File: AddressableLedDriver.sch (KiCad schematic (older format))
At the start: 23 parts

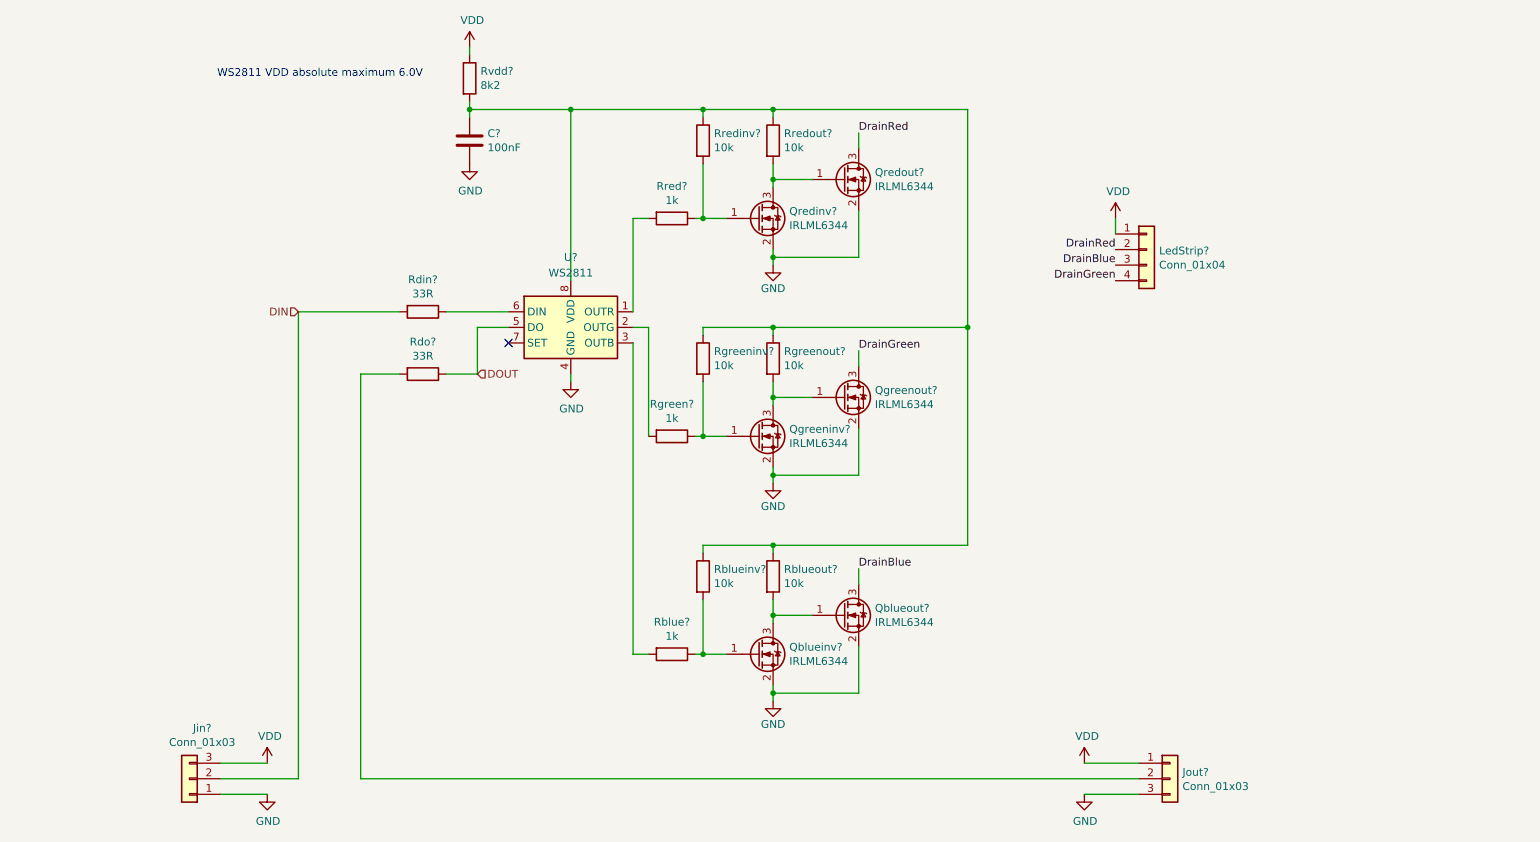
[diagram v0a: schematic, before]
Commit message: Restructure schema
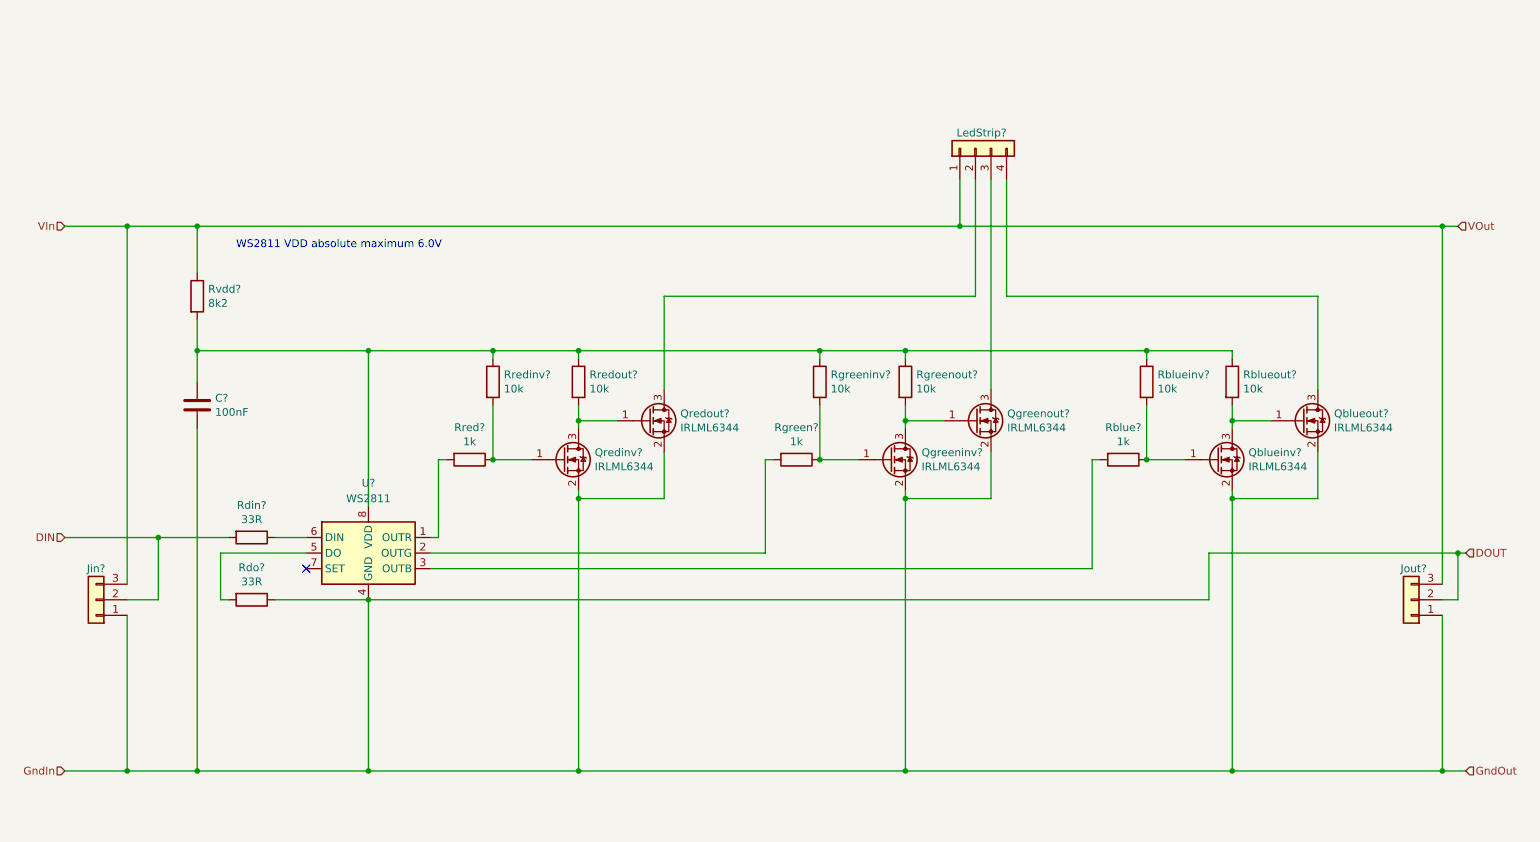
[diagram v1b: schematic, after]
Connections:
- net DOUT: now also C?.2, Jin?.1 (Pin_1), Jout?.1 (Pin_1), Jout?.2 (Pin_2), Qblueinv?.2 (S), Qblueout?.2 (S), Qgreeninv?.2 (S), Qgreenout?.2 (S), Qredinv?.2 (S), Qredout?.2 (S), U?.4 (GND); no longer U?.5 (DO)
- net at Rdo?.2: now also U?.5 (DO); no longer Jout?.2 (Pin_2)
- net DrainBlue: no longer names the net of LedStrip?.3 (Pin_3)
- net DrainBlue: now also Qgreenout?.3 (D); no longer Qblueout?.3 (D)
- net DrainGreen: no longer names the net of LedStrip?.4 (Pin_4)
- net DrainGreen: now also Qblueout?.3 (D); no longer Qgreenout?.3 (D)
- net DrainRed: no longer names the net of LedStrip?.2 (Pin_2), Qredout?.3 (D)
- removed net GND: C?.2, Jin?.1 (Pin_1), Jout?.3 (Pin_3), Qblueinv?.2 (S), Qblueout?.2 (S), Qgreeninv?.2 (S), Qgreenout?.2 (S), Qredinv?.2 (S), Qredout?.2 (S), U?.4 (GND)
- net VDD renamed VIn
- net VIn: now also Jout?.3 (Pin_3); no longer Jout?.1 (Pin_1)
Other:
- moved on the sheet: C?, Jin?, Jout?, LedStrip?, Qblueinv?, Qblueout?, Qgreeninv?, Qgreenout?, Qredinv?, Qredout?, Rblue?, Rblueinv?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

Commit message: Add array of LED Driver
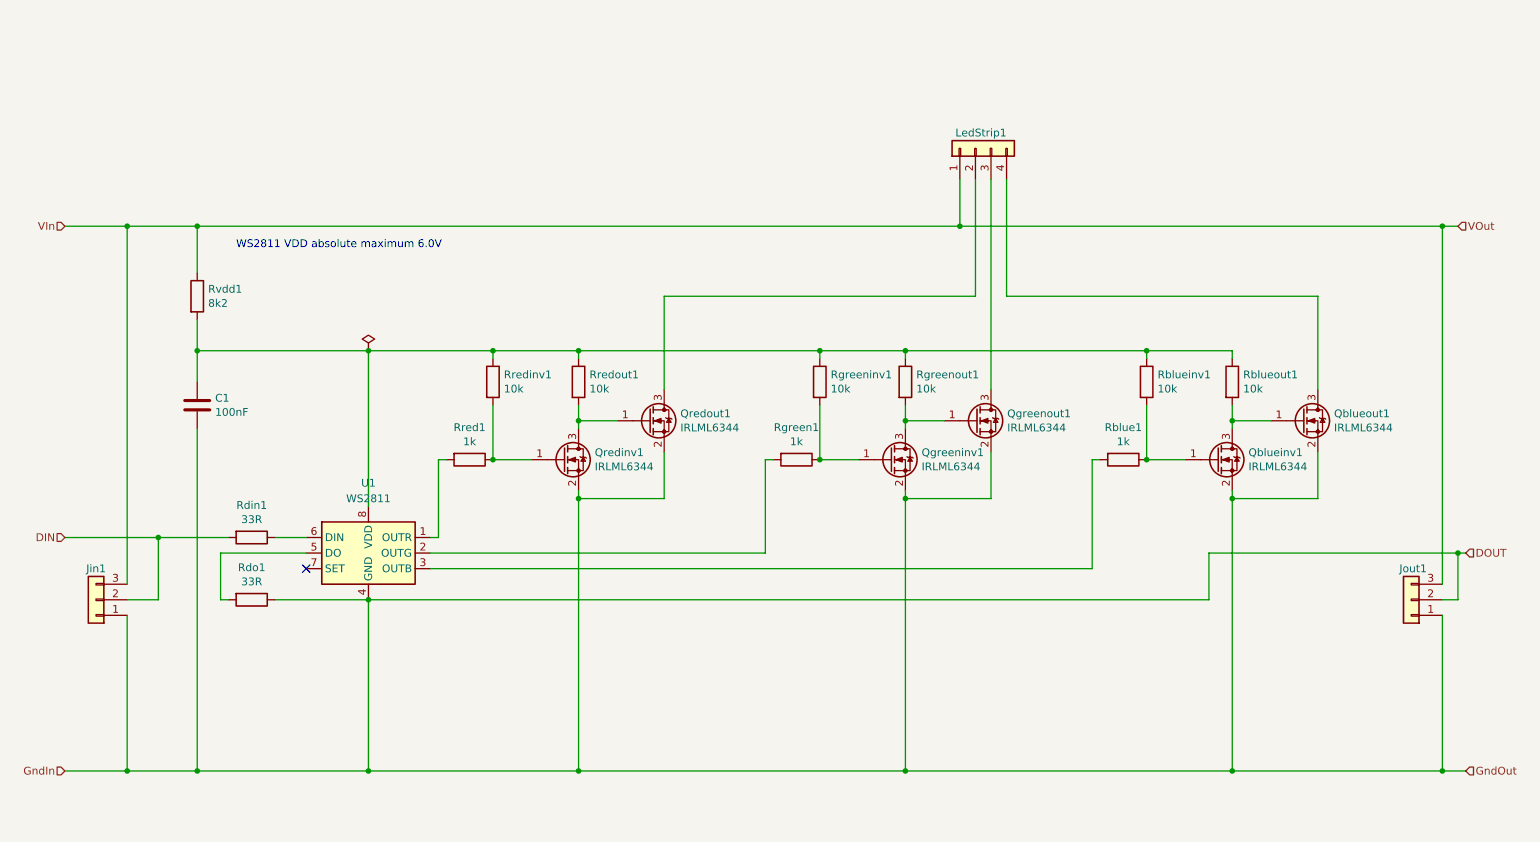
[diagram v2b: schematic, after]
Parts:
- gave numbers to parts that had none: 23

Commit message: Add footprint to mosfets
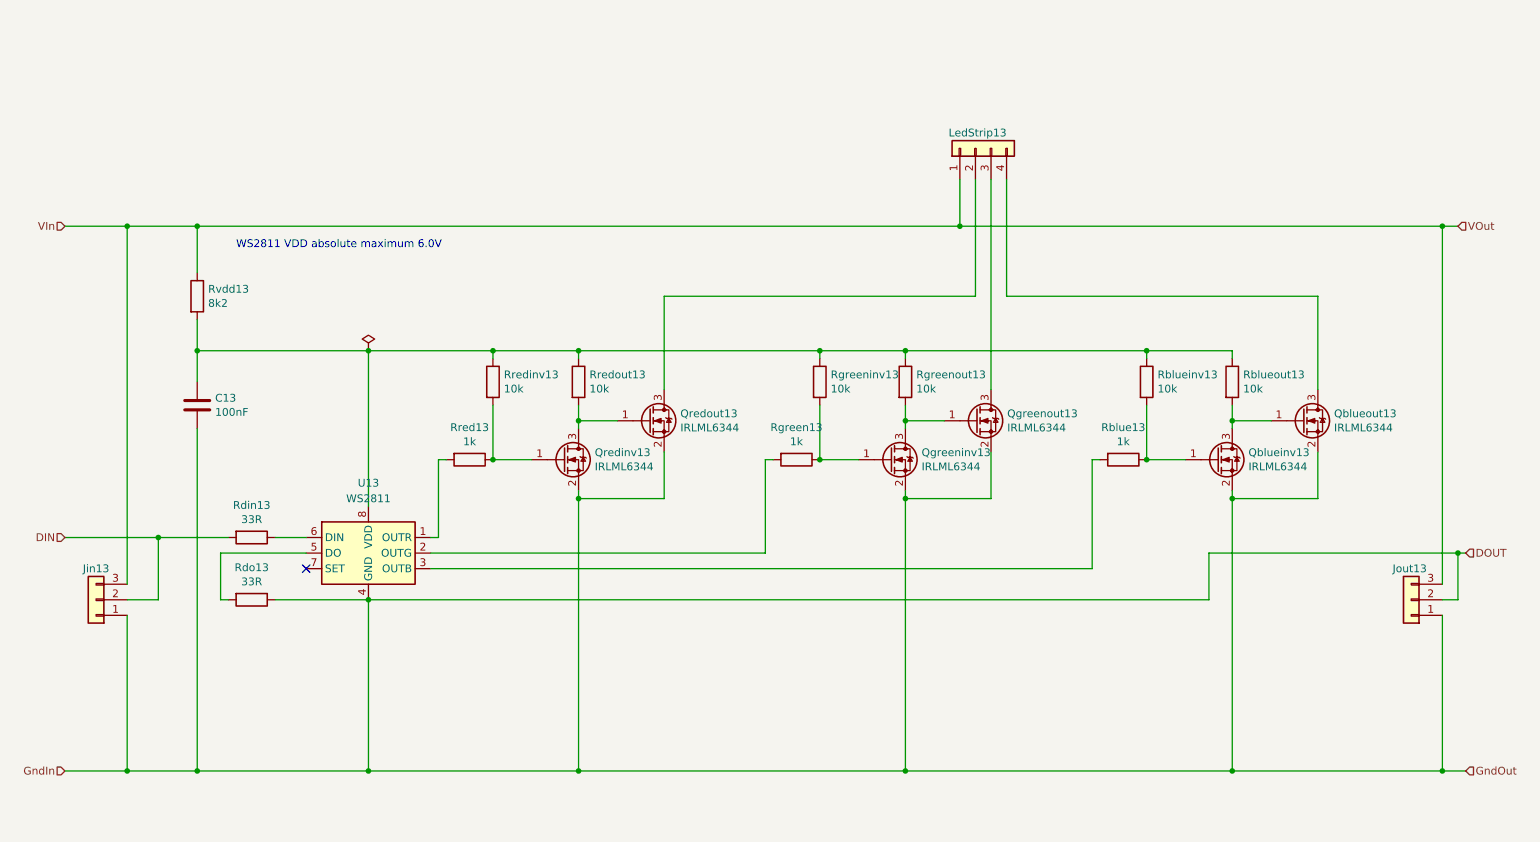
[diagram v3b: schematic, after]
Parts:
- Qblueinv1, Qblueout1, Qgreeninv1, Qgreenout1, Qredinv1, Qredout1: footprint Package_TO_SOT_SMD:SOT-23 -> TO_SOT_Packages_SMD:SOT-23_Handsoldering
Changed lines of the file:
@@
 $Descr A4 11693 8268
 encoding utf-8
-Sheet 2 17
+Sheet 14 17
 Title ""
 Date ""
@@
 AR Path="/601B7703/6006C523" Ref="Rdin15"  Part="1"
 AR Path="/601B7A66/6006C523" Ref="Rdin16"  Part="1"
-F 0 "Rdin1" V 2493 4300 50  0000 C CNN
+F 0 "Rdin13" V 2493 4300 50  0000 C CNN
 F 1 "33R" V 2584 4300 50  0000 C CNN
 F 2 "Capacitors_SMD:C_0603_HandSoldering" V 2630 4300 50  0001 C CNN
@@
 AR Path="/601B7703/6006C530" Ref="Rdo15"  Part="1"
 AR Path="/601B7A66/6006C530" Ref="Rdo16"  Part="1"
-F 0 "Rdo1" V 2493 4700 50  0000 C CNN
+F 0 "Rdo13" V 2493 4700 50  0000 C CNN
 F 1 "33R" V 2584 4700 50  0000 C CNN
 F 2 "Capacitors_SMD:C_0603_HandSoldering" V 2630 4700 50  0001 C CNN
@@
 AR Path="/601B7703/6006C537" Ref="Rredout15"  Part="1"
 AR Path="/601B7A66/6006C537" Ref="Rredout16"  Part="1"
-F 0 "Rredout1" H 4870 3346 50  0000 L CNN
+F 0 "Rredout13" H 4870 3346 50  0000 L CNN
 F 1 "10k" H 4870 3255 50  0000 L CNN
 F 2 "Capacitors_SMD:C_0603_HandSoldering" V 4730 3300 50  0001 C CNN
@@
 AR Path="/601B7703/6006C543" Ref="Rred15"  Part="1"
 AR Path="/601B7A66/6006C543" Ref="Rred16"  Part="1"
-F 0 "Rred1" V 3893 3800 50  0000 C CNN
+F 0 "Rred13" V 3893 3800 50  0000 C CNN
 F 1 "1k" V 3984 3800 50  0000 C CNN
 F 2 "Capacitors_SMD:C_0603_HandSoldering" V 4030 3800 50  0001 C CNN
@@
 AR Path="/601B7703/6006C549" Ref="Rredinv15"  Part="1"
 AR Path="/601B7A66/6006C549" Ref="Rredinv16"  Part="1"
-F 0 "Rredinv1" H 4320 3346 50  0000 L CNN
+F 0 "Rredinv13" H 4320 3346 50  0000 L CNN
 F 1 "10k" H 4320 3255 50  0000 L CNN
 F 2 "Capacitors_SMD:C_0603_HandSoldering" V 4180 3300 50  0001 C CNN
@@
 AR Path="/601B7703/6006C553" Ref="Qredinv15"  Part="1"
 AR Path="/601B7A66/6006C553" Ref="Qredinv16"  Part="1"
-F 0 "Qredinv1" H 4904 3846 50  0000 L CNN
+F 0 "Qredinv13" H 4904 3846 50  0000 L CNN
 F 1 "IRLML6344" H 4904 3755 50  0000 L CNN
-F 2 "Package_TO_SOT_SMD:SOT-23" H 4900 3710 50  0001 L CIN
+F 2 "TO_SOT_Packages_SMD:SOT-23_Handsoldering" H 4900 3710 50  0001 L CIN
 F 3 "http://www.farnell.com/datasheets/1911844.pdf" H 4700 3800 50  0001 L CNN
 F 4 "IRLML6344TRPbF" H 5220 3610 50  0001 C CNN "Orderable part number"
@@
 AR Path="/601B7703/6006C559" Ref="U15"  Part="1"
 AR Path="/601B7A66/6006C559" Ref="U16"  Part="1"
-F 0 "U1" H 3450 4850 50  0000 C CNN
+F 0 "U13" H 3450 4850 50  0000 C CNN
 F 1 "WS2811" H 3450 4750 50  0000 C CNN
 F 2 "Housings_SOIC:SOIC-8_3.9x4.9mm_Pitch1.27mm" H 3150 4550 50  0001 C CNN
@@
 AR Path="/601B7703/6006C573" Ref="Rvdd15"  Part="1"
 AR Path="/601B7A66/6006C573" Ref="Rvdd16"  Part="1"
-F 0 "Rvdd1" H 2420 2796 50  0000 L CNN
+F 0 "Rvdd13" H 2420 2796 50  0000 L CNN
 F 1 "8k2" H 2420 2705 50  0000 L CNN
 F 2 "Capacitors_SMD:C_0603_HandSoldering" V 2280 2750 50  0001 C CNN
@@
 AR Path="/601B7703/6006C579" Ref="C15"  Part="1"
 AR Path="/601B7A66/6006C579" Ref="C16"  Part="1"
-F 0 "C1" H 2465 3496 50  0000 L CNN
+F 0 "C13" H 2465 3496 50  0000 L CNN
 F 1 "100nF" H 2465 3405 50  0000 L CNN
 F 2 "Capacitors_SMD:C_0603_HandSoldering" H 2388 3300 50  0001 C CNN
@@
 AR Path="/601B7703/6006C593" Ref="Qredout15"  Part="1"
 AR Path="/601B7A66/6006C593" Ref="Qredout16"  Part="1"
-F 0 "Qredout1" H 5454 3596 50  0000 L CNN
+F 0 "Qredout13" H 5454 3596 50  0000 L CNN
 F 1 "IRLML6344" H 5454 3505 50  0000 L CNN
-F 2 "Package_TO_SOT_SMD:SOT-23" H 5450 3460 50  0001 L CIN
+F 2 "TO_SOT_Packages_SMD:SOT-23_Handsoldering" H 5450 3460 50  0001 L CIN
 F 3 "http://www.farnell.com/datasheets/1911844.pdf" H 5250 3550 50  0001 L CNN
 F 4 "IRLML6344TRPbF" H 5770 3360 50  0001 C CNN "Orderable part number"
@@
 AR Path="/601B7703/6006C59C" Ref="Rgreenout15"  Part="1"
 AR Path="/601B7A66/6006C59C" Ref="Rgreenout16"  Part="1"
-F 0 "Rgreenout1" H 6970 3346 50  0000 L CNN
+F 0 "Rgreenout13" H 6970 3346 50  0000 L CNN
 F 1 "10k" H 6970 3255 50  0000 L CNN
 F 2 "Capacitors_SMD:C_0603_HandSoldering" V 6830 3300 50  0001 C CNN
@@
 AR Path="/601B7703/6006C5A8" Ref="Rgreen15"  Part="1"
 AR Path="/601B7A66/6006C5A8" Ref="Rgreen16"  Part="1"
-F 0 "Rgreen1" V 5993 3800 50  0000 C CNN
+F 0 "Rgreen13" V 5993 3800 50  0000 C CNN
 F 1 "1k" V 6084 3800 50  0000 C CNN
 F 2 "Capacitors_SMD:C_0603_HandSoldering" V 6130 3800 50  0001 C CNN
@@
 AR Path="/601B7703/6006C5AE" Ref="Rgreeninv15"  Part="1"
 AR Path="/601B7A66/6006C5AE" Ref="Rgreeninv16"  Part="1"
-F 0 "Rgreeninv1" H 6420 3346 50  0000 L CNN
+F 0 "Rgreeninv13" H 6420 3346 50  0000 L CNN
 F 1 "10k" H 6420 3255 50  0000 L CNN
 F 2 "Capacitors_SMD:C_0603_HandSoldering" V 6280 3300 50  0001 C CNN
@@
 AR Path="/601B7703/6006C5B8" Ref="Qgreeninv15"  Part="1"
 AR Path="/601B7A66/6006C5B8" Ref="Qgreeninv16"  Part="1"
-F 0 "Qgreeninv1" H 7004 3846 50  0000 L CNN
+F 0 "Qgreeninv13" H 7004 3846 50  0000 L CNN
 F 1 "IRLML6344" H 7004 3755 50  0000 L CNN
-F 2 "Package_TO_SOT_SMD:SOT-23" H 7000 3710 50  0001 L CIN
+F 2 "TO_SOT_Packages_SMD:SOT-23_Handsoldering" H 7000 3710 50  0001 L CIN
 F 3 "http://www.farnell.com/datasheets/1911844.pdf" H 6800 3800 50  0001 L CNN
 F 4 "IRLML6344TRPbF" H 7320 3610 50  0001 C CNN "Orderable part number"
@@
 AR Path="/601B7703/6006C5D4" Ref="Qgreenout15"  Part="1"
 AR Path="/601B7A66/6006C5D4" Ref="Qgreenout16"  Part="1"
-F 0 "Qgreenout1" H 7554 3596 50  0000 L CNN
+F 0 "Qgreenout13" H 7554 3596 50  0000 L CNN
 F 1 "IRLML6344" H 7554 3505 50  0000 L CNN
-F 2 "Package_TO_SOT_SMD:SOT-23" H 7550 3460 50  0001 L CIN
+F 2 "TO_SOT_Packages_SMD:SOT-23_Handsoldering" H 7550 3460 50  0001 L CIN
 F 3 "http://www.farnell.com/datasheets/1911844.pdf" H 7350 3550 50  0001 L CNN
 F 4 "IRLML6344TRPbF" H 7870 3360 50  0001 C CNN "Orderable part number"
@@
 AR Path="/601B7703/6006C5DA" Ref="Rblueout15"  Part="1"
 AR Path="/601B7A66/6006C5DA" Ref="Rblueout16"  Part="1"
-F 0 "Rblueout1" H 9070 3346 50  0000 L CNN
+F 0 "Rblueout13" H 9070 3346 50  0000 L CNN
 F 1 "10k" H 9070 3255 50  0000 L CNN
 F 2 "Capacitors_SMD:C_0603_HandSoldering" V 8930 3300 50  0001 C CNN
@@
 AR Path="/601B7703/6006C5E6" Ref="Rblue15"  Part="1"
 AR Path="/601B7A66/6006C5E6" Ref="Rblue16"  Part="1"
-F 0 "Rblue1" V 8093 3800 50  0000 C CNN
+F 0 "Rblue13" V 8093 3800 50  0000 C CNN
 F 1 "1k" V 8184 3800 50  0000 C CNN
 F 2 "Capacitors_SMD:C_0603_HandSoldering" V 8230 3800 50  0001 C CNN
@@
 AR Path="/601B7703/6006C5EC" Ref="Rblueinv15"  Part="1"
 AR Path="/601B7A66/6006C5EC" Ref="Rblueinv16"  Part="1"
-F 0 "Rblueinv1" H 8520 3346 50  0000 L CNN
+F 0 "Rblueinv13" H 8520 3346 50  0000 L CNN
 F 1 "10k" H 8520 3255 50  0000 L CNN
 F 2 "Capacitors_SMD:C_0603_HandSoldering" V 8380 3300 50  0001 C CNN
@@
 AR Path="/601B7703/6006C5F6" Ref="Qblueinv15"  Part="1"
 AR Path="/601B7A66/6006C5F6" Ref="Qblueinv16"  Part="1"
-F 0 "Qblueinv1" H 9104 3846 50  0000 L CNN
+F 0 "Qblueinv13" H 9104 3846 50  0000 L CNN
 F 1 "IRLML6344" H 9104 3755 50  0000 L CNN
-F 2 "Package_TO_SOT_SMD:SOT-23" H 9100 3710 50  0001 L CIN
+F 2 "TO_SOT_Packages_SMD:SOT-23_Handsoldering" H 9100 3710 50  0001 L CIN
 F 3 "http://www.farnell.com/datasheets/1911844.pdf" H 8900 3800 50  0001 L CNN
 F 4 "IRLML6344TRPbF" H 9420 3610 50  0001 C CNN "Orderable part number"
@@
 AR Path="/601B7703/6006C612" Ref="Qblueout15"  Part="1"
 AR Path="/601B7A66/6006C612" Ref="Qblueout16"  Part="1"
-F 0 "Qblueout1" H 9654 3596 50  0000 L CNN
+F 0 "Qblueout13" H 9654 3596 50  0000 L CNN
 F 1 "IRLML6344" H 9654 3505 50  0000 L CNN
-F 2 "Package_TO_SOT_SMD:SOT-23" H 9650 3460 50  0001 L CIN
+F 2 "TO_SOT_Packages_SMD:SOT-23_Handsoldering" H 9650 3460 50  0001 L CIN
 F 3 "http://www.farnell.com/datasheets/1911844.pdf" H 9450 3550 50  0001 L CNN
 F 4 "IRLML6344TRPbF" H 9970 3360 50  0001 C CNN "Orderable part number"
@@
 AR Path="/601B7703/6006C62D" Ref="LedStrip15"  Part="1"
 AR Path="/601B7A66/6006C62D" Ref="LedStrip16"  Part="1"
-F 0 "LedStrip1" V 7450 1600 50  0000 L CNN
+F 0 "LedStrip13" V 7450 1600 50  0000 L CNN
 F 1 "Conn_01x04" V 7450 1500 50  0001 L CNN
 F 2 "StripArray:RGB_Strip" H 7350 1800 50  0001 C CNN
@@
 AR Path="/601B7703/6006C642" Ref="Jout15"  Part="1"
 AR Path="/601B7A66/6006C642" Ref="Jout16"  Part="1"
-F 0 "Jout1" H 10050 4500 50  0000 L CNN
+F 0 "Jout13" H 10050 4500 50  0000 L CNN
 F 1 "Conn_01x03" H 10230 4651 50  0001 L CNN
 F 2 "Pin_Headers:Pin_Header_Straight_1x03_Pitch2.54mm" H 10150 4700 50  0001 C CNN
@@
 AR Path="/601B7703/6006C63C" Ref="Jin15"  Part="1"
 AR Path="/601B7A66/6006C63C" Ref="Jin16"  Part="1"
-F 0 "Jin1" H 1700 4500 50  0000 C CNN
+F 0 "Jin13" H 1700 4500 50  0000 C CNN
 F 1 "Conn_01x03" H 1618 4466 50  0001 C CNN
 F 2 "Pin_Headers:Pin_Header_Straight_1x03_Pitch2.54mm" H 1700 4700 50  0001 C CNN
@@
 AR Path="/601B7703/601B0CCE" Ref="#FLG013"  Part="1"
 AR Path="/601B7A66/601B0CCE" Ref="#FLG014"  Part="1"
-F 0 "#FLG0103" H 3450 3175 50  0001 C CNN
+F 0 "#FLG011" H 3450 3175 50  0001 C CNN
 F 1 "PWR_FLAG" H 3450 3273 50  0001 C CNN
 F 2 "" H 3450 3100 50  0001 C CNN
